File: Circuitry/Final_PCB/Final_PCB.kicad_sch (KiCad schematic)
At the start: 110 parts, among them Q1 Q_Dual_NMOS_S1G1D2S2G2D1, Q2 Q_Dual_NMOS_S1G1D2S2G2D1, Q3 Q_Dual_NMOS_S1G1D2S2G2D1, Q4 Q_Dual_NMOS_S1G1D2S2G2D1, Q5 Q_Dual_NMOS_S1G1D2S2G2D1, Q6 Q_Dual_NMOS_S1G1D2S2G2D1, Q7 Q_Dual_NMOS_S1G1D2S2G2D1, Q8 Q_Dual_NMOS_S1G1D2S2G2D1, SW1 SW_SPST, SW2 SW_SPST

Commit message: code updates + housing faceplate 2
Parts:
- SW1, SW2: footprint (none) -> Resistor_THT:R_Axial_DIN0207_L6.3mm_D2.5mm_P5.08mm_Vertical
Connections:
- net 5V_GND_ARD1 is gone; now on net 12V_GND: ARD1_SOURCE1.2 (Pin_2), C1.2, C2.2, C3.2, C4.2, C5.2, C6.2, IFD97_1.1 (Pin_1), IFD97_1.3 (Pin_3), IFD97_2.1 (Pin_1), IFD97_2.3 (Pin_3), IFE91D_1.2 (Pin_2), IFE91D_2.2 (Pin_2), OP07C_1.4 (Pin_4), OP07C_2.4 (Pin_4), R2.2, R6.2, SW1.2 (B), SW2.2 (B)
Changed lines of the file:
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@@
   (junction (at 377.19 123.19) (diameter 0) (color 0 0 0 0)
   )
+  (junction (at 485.14 143.51) (diameter 0) (color 0 0 0 0)
+  )
   (junction (at 346.71 171.45) (diameter 0) (color 0 0 0 0)
   )
@@
     (stroke (width 0) (type default))
   )
+  (wire (pts (xy 485.14 143.51) (xy 485.14 148.59))
+    (stroke (width 0) (type default))
+  )
   (wire (pts (xy 372.11 325.12) (xy 377.19 325.12))
     (stroke (width 0) (type default))
@@
   )
   (label "+12V" (at 392.43 205.74 0) (fields_autoplaced)
+    (effects (font (size 1.27 1.27)) (justify left bottom))
+  )
+  (label "5V_GND_ARD2" (at 485.14 148.59 0) (fields_autoplaced)
     (effects (font (size 1.27 1.27)) (justify left bottom))
   )
@@
       (effects (font (size 1.27 1.27)))
     )
-    (property "Footprint" "" (at 586.74 184.15 0)
+    (property "Footprint" "Resistor_THT:R_Axial_DIN0207_L6.3mm_D2.5mm_P5.08mm_Vertical" (at 586.74 184.15 0)
       (effects (font (size 1.27 1.27)) hide)
     )
@@
       (effects (font (size 1.27 1.27)))
     )
-    (property "Footprint" "" (at 543.56 182.88 0)
-      (effects (font (size 1.27 1.27)) hide)
-    )
+    (property "Footprint" "Resistor_THT:R_Axial_DIN0207_L6.3mm_D2.5mm_P5.08mm_Vertical" (at 543.56 182.88 0)
+      (effects (font (size 1.27 1.27)) hide)
+    )

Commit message: final pcb and code updates
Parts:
- removed SW1, SW2: SW_SPST, Resistor_THT:R_Axial_DIN0207_L6.3mm_D2.5mm_P5.08mm_Vertical, symbol Switch:SW_SPST
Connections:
- net 12V_GND: now also LEDSPT1.2 (Pin_2), LEDSPT2.2 (Pin_2)
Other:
- moved on the sheet: SOLENOID1
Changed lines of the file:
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@@
   (junction (at 372.11 332.74) (diameter 0) (color 0 0 0 0)
   )
+  (junction (at 313.69 247.65) (diameter 0) (color 0 0 0 0)
+  )
   (junction (at 372.11 304.8) (diameter 0) (color 0 0 0 0)
   )
@@
   (junction (at 370.84 247.65) (diameter 0) (color 0 0 0 0)
   )
-  (junction (at 316.23 247.65) (diameter 0) (color 0 0 0 0)
-  )
-  (junction (at 316.23 240.03) (diameter 0) (color 0 0 0 0)
-  )
   (junction (at 502.92 304.8) (diameter 0) (color 0 0 0 0)
   )
@@
   (junction (at 436.88 247.65) (diameter 0) (color 0 0 0 0)
   )
+  (junction (at 320.04 238.76) (diameter 0) (color 0 0 0 0)
+  )
   (junction (at 519.43 143.51) (diameter 0) (color 0 0 0 0)
   )
@@
     (stroke (width 0) (type default))
   )
+  (wire (pts (xy 313.69 238.76) (xy 320.04 238.76))
+    (stroke (width 0) (type default))
+  )
   (wire (pts (xy 295.91 222.25) (xy 308.61 222.25))
     (stroke (width 0) (type default))
@@
     (stroke (width 0) (type default))
   )
-  (wire (pts (xy 316.23 240.03) (xy 321.31 240.03))
+  (wire (pts (xy 320.04 238.76) (xy 320.04 245.11))
     (stroke (width 0) (type default))
   )
@@
     (stroke (width 0) (type default))
   )
-  (wire (pts (xy 548.64 182.88) (xy 554.99 182.88))
-    (stroke (width 0) (type default))
-  )
   (wire (pts (xy 317.5 304.8) (xy 322.58 304.8))
     (stroke (width 0) (type default))
@@
     (stroke (width 0) (type default))
   )
-  (wire (pts (xy 581.66 184.15) (xy 575.31 184.15))
-    (stroke (width 0) (type default))
-  )
   (wire (pts (xy 347.98 123.19) (xy 347.98 129.54))
     (stroke (width 0) (type default))
@@
     (stroke (width 0) (type default))
   )
-  (wire (pts (xy 316.23 247.65) (xy 321.31 247.65))
-    (stroke (width 0) (type default))
-  )
   (wire (pts (xy 488.95 311.15) (xy 488.95 309.88))
     (stroke (width 0) (type default))
@@
     (stroke (width 0) (type default))
   )
+  (wire (pts (xy 313.69 247.65) (xy 320.04 247.65))
+    (stroke (width 0) (type default))
+  )
   (wire (pts (xy 496.57 275.59) (xy 501.65 275.59))
     (stroke (width 0) (type default))
@@
     (stroke (width 0) (type default))
   )
-  (wire (pts (xy 311.15 247.65) (xy 316.23 247.65))
+  (wire (pts (xy 311.15 247.65) (xy 313.69 247.65))
     (stroke (width 0) (type default))
   )
@@
     (stroke (width 0) (type default))
   )
-  (wire (pts (xy 591.82 184.15) (xy 596.9 184.15))
+  (wire (pts (xy 575.31 184.15) (xy 596.9 184.15))
     (stroke (width 0) (type default))
   )
@@
     (stroke (width 0) (type default))
   )
-  (wire (pts (xy 538.48 182.88) (xy 532.13 182.88))
+  (wire (pts (xy 532.13 182.88) (xy 554.99 182.88))
     (stroke (width 0) (type default))
   )
@@
     (stroke (width 0) (type default))
   )
-  (wire (pts (xy 316.23 237.49) (xy 316.23 240.03))
+  (wire (pts (xy 320.04 237.49) (xy 320.04 238.76))
     (stroke (width 0) (type default))
   )
@@
     (stroke (width 0) (type default))
   )
-  (wire (pts (xy 321.31 247.65) (xy 321.31 242.57))
-    (stroke (width 0) (type default))
-  )
   (wire (pts (xy 334.01 193.04) (xy 334.01 196.85))
     (stroke (width 0) (type default))
@@
     (stroke (width 0) (type default))
   )
+  (wire (pts (xy 313.69 246.38) (xy 313.69 247.65))
+    (stroke (width 0) (type default))
+  )
   (wire (pts (xy 424.18 281.94) (xy 424.18 280.67))
     (stroke (width 0) (type default))
@@
     (effects (font (size 1.27 1.27)) (justify left bottom))
   )
-  (label "+12V" (at 316.23 237.49 0) (fields_autoplaced)
+  (label "+12V" (at 320.04 237.49 0) (fields_autoplaced)
     (effects (font (size 1.27 1.27)) (justify left bottom))
   )
@@
     )
   )
-  (symbol (lib_id "Diode:MBR0540") (at 316.23 243.84 90) (mirror x) (unit 1)
-    (in_bom yes) (on_board yes) (dnp no)
-    (property "Reference" "D1" (at 313.69 242.2525 90)
-      (effects (font (size 1.27 1.27)) (justify left))
-    )
-    (property "Value" "MBR0540" (at 313.69 244.7925 90)
-      (effects (font (size 1.27 1.27)) (justify left))
-    )
-    (property "Footprint" "Diode_SMD:D_SOD-123" (at 320.675 243.84 0)
-      (effects (font (size 1.27 1.27)) hide)
-    )
-    (property "Datasheet" "http://www.mccsemi.com/up_pdf/MBR0520~MBR0580(SOD123).pdf" (at 316.23 243.84 0)
-      (effects (font (size 1.27 1.27)) hide)
-    )
-    (pin "1")
-    (pin "2")
-    (instances
-      (project "Final_PCB"
-        (path "/3aa8d99f-bc88-4d2c-936c-bff7aa7008c1"
-          (reference "D1") (unit 1)
-        )
-      )
-    )
-  )
   (symbol (lib_id "Connector_Generic:Conn_02x08_Counter_Clockwise") (at 313.69 217.17 0) (unit 1)
     (in_bom yes) (on_board yes) (dnp no) (fields_autoplaced)
@@
     )
   )
-  (symbol (lib_id "Connector_Generic:Conn_01x02") (at 326.39 240.03 0) (unit 1)
+  (symbol (lib_id "Connector_Generic:Conn_01x02") (at 325.12 245.11 0) (unit 1)
     (in_bom yes) (on_board yes) (dnp no)
-    (property "Reference" "SOLENOID1" (at 326.39 246.38 0)
+    (property "Reference" "SOLENOID1" (at 325.12 251.46 0)
       (effects (font (size 1.27 1.27)))
     )
-    (property "Value" "Conn_01x02" (at 325.12 245.11 90)
+    (property "Value" "Conn_01x02" (at 323.85 250.19 90)
       (effects (font (size 1.27 1.27)) (justify right) hide)
     )
-    (property "Footprint" "Resistor_THT:R_Axial_DIN0207_L6.3mm_D2.5mm_P5.08mm_Vertical" (at 326.39 240.03 0)
+    (property "Footprint" "Resistor_THT:R_Axial_DIN0207_L6.3mm_D2.5mm_P5.08mm_Vertical" (at 325.12 245.11 0)
       (effects (font (size 1.27 1.27)) hide)
     )
-    (property "Datasheet" "~" (at 326.39 240.03 0)
+    (property "Datasheet" "~" (at 325.12 245.11 0)
       (effects (font (size 1.27 1.27)) hide)
     )
@@
     )
   )
-  (symbol (lib_id "Switch:SW_SPST") (at 586.74 184.15 0) (unit 1)
-    (in_bom yes) (on_board yes) (dnp no)
-    (property "Reference" "SW2" (at 586.74 177.8 0)
-      (effects (font (size 1.27 1.27)))
-    )
-    (property "Value" "SW_SPST" (at 586.74 180.34 0)
-      (effects (font (size 1.27 1.27)))
-    )
-    (property "Footprint" "Resistor_THT:R_Axial_DIN0207_L6.3mm_D2.5mm_P5.08mm_Vertical" (at 586.74 184.15 0)
-      (effects (font (size 1.27 1.27)) hide)
-    )
-    (property "Datasheet" "~" (at 586.74 184.15 0)
-      (effects (font (size 1.27 1.27)) hide)
-    )
-    (pin "1")
-    (pin "2")
-    (instances
-      (project "Final_PCB"
-        (path "/3aa8d99f-bc88-4d2c-936c-bff7aa7008c1"
-          (reference "SW2") (unit 1)
-        )
-      )
-    )
-  )
   (symbol (lib_id "Connector_Generic:Conn_01x01") (at 330.2 365.76 270) (unit 1)
     (in_bom yes) (on_board yes) (dnp no) (fields_autoplaced)
@@
     )
   )
-  (symbol (lib_id "Switch:SW_SPST") (at 543.56 182.88 0) (unit 1)
-    (in_bom yes) (on_board yes) (dnp no) (fields_autoplaced)
-    (property "Reference" "SW1" (at 543.56 176.53 0)
-      (effects (font (size 1.27 1.27)))
-    )
-    (property "Value" "SW_SPST" (at 543.56 179.07 0)
-      (effects (font (size 1.27 1.27)))
-    )
-    (property "Footprint" "Resistor_THT:R_Axial_DIN0207_L6.3mm_D2.5mm_P5.08mm_Vertical" (at 543.56 182.88 0)
-      (effects (font (size 1.27 1.27)) hide)
-    )
-    (property "Datasheet" "~" (at 543.56 182.88 0)
-      (effects (font (size 1.27 1.27)) hide)
-    )
-    (pin "1")
-    (pin "2")
-    (instances
-      (project "Final_PCB"
-        (path "/3aa8d99f-bc88-4d2c-936c-bff7aa7008c1"
-          (reference "SW1") (unit 1)
-        )
-      )
-    )
-  )
   (symbol (lib_id "Diode:MBR0540") (at 372.11 328.93 90) (mirror x) (unit 1)
     (in_bom yes) (on_board yes) (dnp no)
@@
         )
       )
+    )
+  )
+  (symbol (lib_id "Diode:MBR0540") (at 313.69 242.57 90) (mirror x) (unit 1)
+    (in_bom yes) (on_board yes) (dnp no)
+    (property "Reference" "D1" (at 311.15 240.9825 90)
+      (effects (font (size 1.27 1.27)) (justify left))
+    )
+    (property "Value" "MBR0540" (at 311.15 243.5225 90)
+      (effects (font (size 1.27 1.27)) (justify left))
+    )
+    (property "Footprint" "Diode_SMD:D_SOD-123" (at 318.135 242.57 0)
+      (effects (font (size 1.27 1.27)) hide)
+    )
+    (property "Datasheet" "http://www.mccsemi.com/up_pdf/MBR0520~MBR0580(SOD123).pdf" (at 313.69 242.57 0)
+      (effects (font (size 1.27 1.27)) hide)
+    )
+    (pin "1")
+    (pin "2")
+    (instances
+      (project "Final_PCB"
+        (path "/3aa8d99f-bc88-4d2c-936c-bff7aa7008c1"
+          (reference "D1") (unit 1)
+        )
+      )

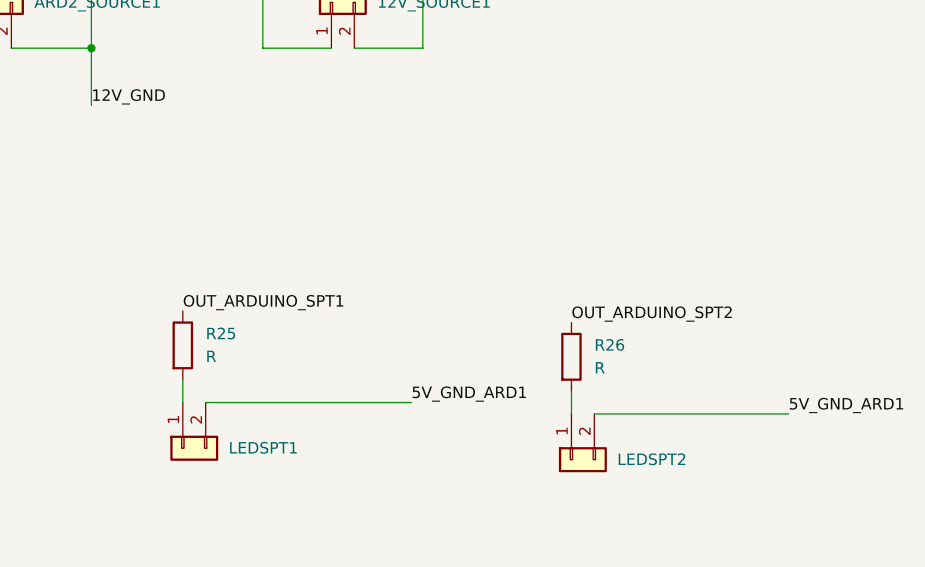
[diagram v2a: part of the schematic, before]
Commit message: final python program version 1st draft, PCB final
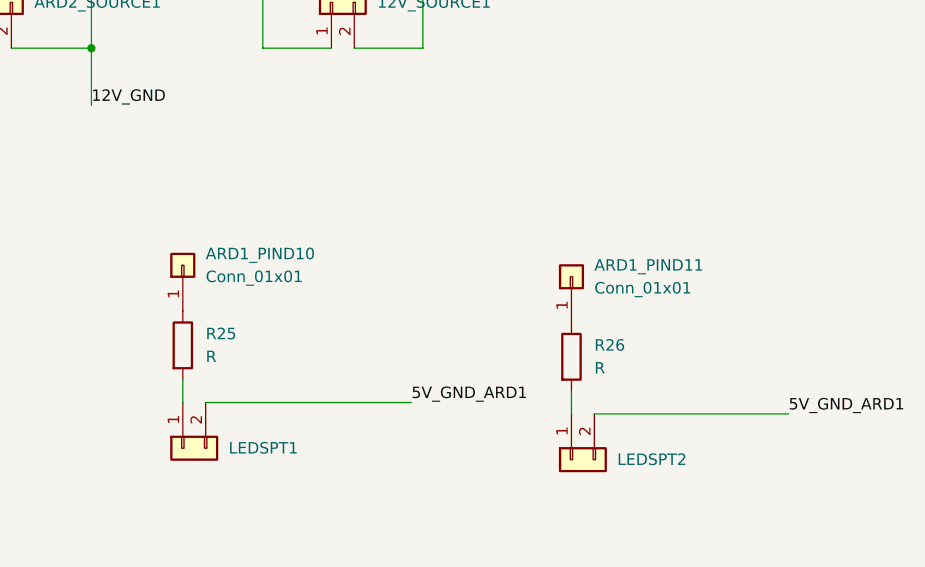
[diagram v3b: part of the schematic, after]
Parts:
- added ARD1_PIND10, ARD1_PIND11: Conn_01x01, Final_PCB_Footprint:ARD_OUT, symbol Connector_Generic:Conn_01x01
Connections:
- net OUT_ARDUINO_SPT1: no longer R25.1
- net OUT_ARDUINO_SPT2: no longer R26.1
- new net: ARD1_PIND11.1 (Pin_1), R26.1
- new net: ARD1_PIND10.1 (Pin_1), R25.1
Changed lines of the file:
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@@
-    (effects (font (size 1.27 1.27)) (justify left bottom))
-  )
-  (label "OUT_ARDUINO_SPT2" (at 572.77 173.99 0) (fields_autoplaced)
     (effects (font (size 1.27 1.27)) (justify left bottom))
   )
@@
   )
   (label "+12V" (at 502.92 322.58 0) (fields_autoplaced)
-    (effects (font (size 1.27 1.27)) (justify left bottom))
-  )
-  (label "OUT_ARDUINO_SPT1" (at 529.59 172.72 0) (fields_autoplaced)
     (effects (font (size 1.27 1.27)) (justify left bottom))
   )
@@
     )
   )
+  (symbol (lib_id "Connector_Generic:Conn_01x01") (at 572.77 168.91 90) (unit 1)
+    (in_bom yes) (on_board yes) (dnp no) (fields_autoplaced)
+    (property "Reference" "ARD1_PIND11" (at 575.31 167.64 90)
+      (effects (font (size 1.27 1.27)) (justify right))
+    )
+    (property "Value" "Conn_01x01" (at 575.31 170.18 90)
+      (effects (font (size 1.27 1.27)) (justify right))
+    )
+    (property "Footprint" "Final_PCB_Footprint:ARD_OUT" (at 572.77 168.91 0)
+      (effects (font (size 1.27 1.27)) hide)
+    )
+    (property "Datasheet" "~" (at 572.77 168.91 0)
+      (effects (font (size 1.27 1.27)) hide)
+    )
+    (pin "1")
+    (instances
+      (project "Final_PCB"
+        (path "/3aa8d99f-bc88-4d2c-936c-bff7aa7008c1"
+          (reference "ARD1_PIND11") (unit 1)
+        )
+      )
+    )
+  )
   (symbol (lib_id "Connector_Generic:Conn_01x01") (at 330.2 365.76 270) (unit 1)
     (in_bom yes) (on_board yes) (dnp no) (fields_autoplaced)
@@
         )
       )
+    )
+  )
+  (symbol (lib_id "Connector_Generic:Conn_01x01") (at 529.59 167.64 90) (unit 1)
+    (in_bom yes) (on_board yes) (dnp no) (fields_autoplaced)
+    (property "Reference" "ARD1_PIND10" (at 532.13 166.37 90)
+      (effects (font (size 1.27 1.27)) (justify right))
+    )
+    (property "Value" "Conn_01x01" (at 532.13 168.91 90)
+      (effects (font (size 1.27 1.27)) (justify right))
+    )
+    (property "Footprint" "Final_PCB_Footprint:ARD_OUT" (at 529.59 167.64 0)
+      (effects (font (size 1.27 1.27)) hide)
+    )
+    (property "Datasheet" "~" (at 529.59 167.64 0)
+      (effects (font (size 1.27 1.27)) hide)
+    )
+    (pin "1")
+    (instances
+      (project "Final_PCB"
+        (path "/3aa8d99f-bc88-4d2c-936c-bff7aa7008c1"
+          (reference "ARD1_PIND10") (unit 1)
+        )
+      )
